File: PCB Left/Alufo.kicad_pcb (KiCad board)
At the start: 2 copper layers, 282.6 x 90.9 mm, 91 parts, among them J1 USB_C_Receptacle_USB2.0_16P_2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, J3 USB_C_Receptacle_USB2.0_16P_2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, K11 PG1350, K12 PG1350, K13 PG1350, K14 PG1350, K15 PG1350, K16 PG1350, K21 PG1350, K22 PG1350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

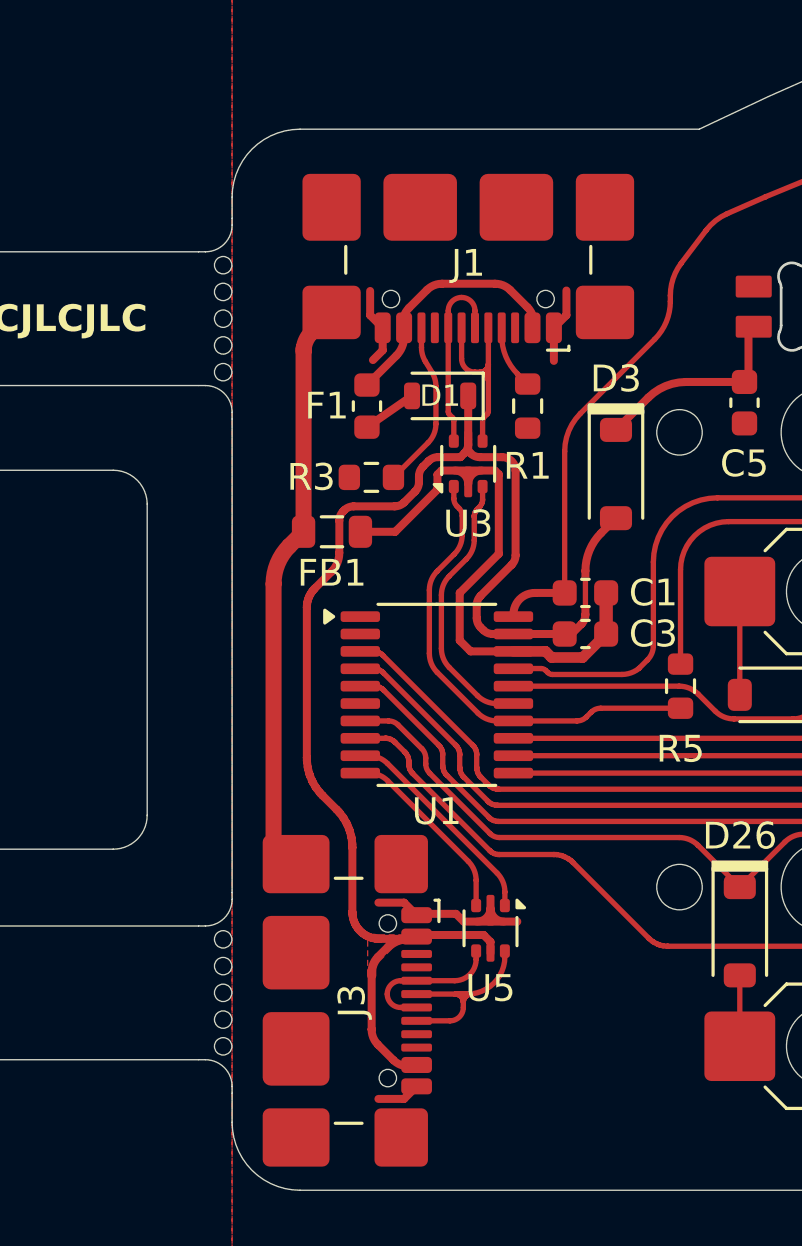
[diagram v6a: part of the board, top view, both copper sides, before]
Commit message: Update extra USB port solder pad
The pad should now not overlap with parts of the port casing that have no metal.
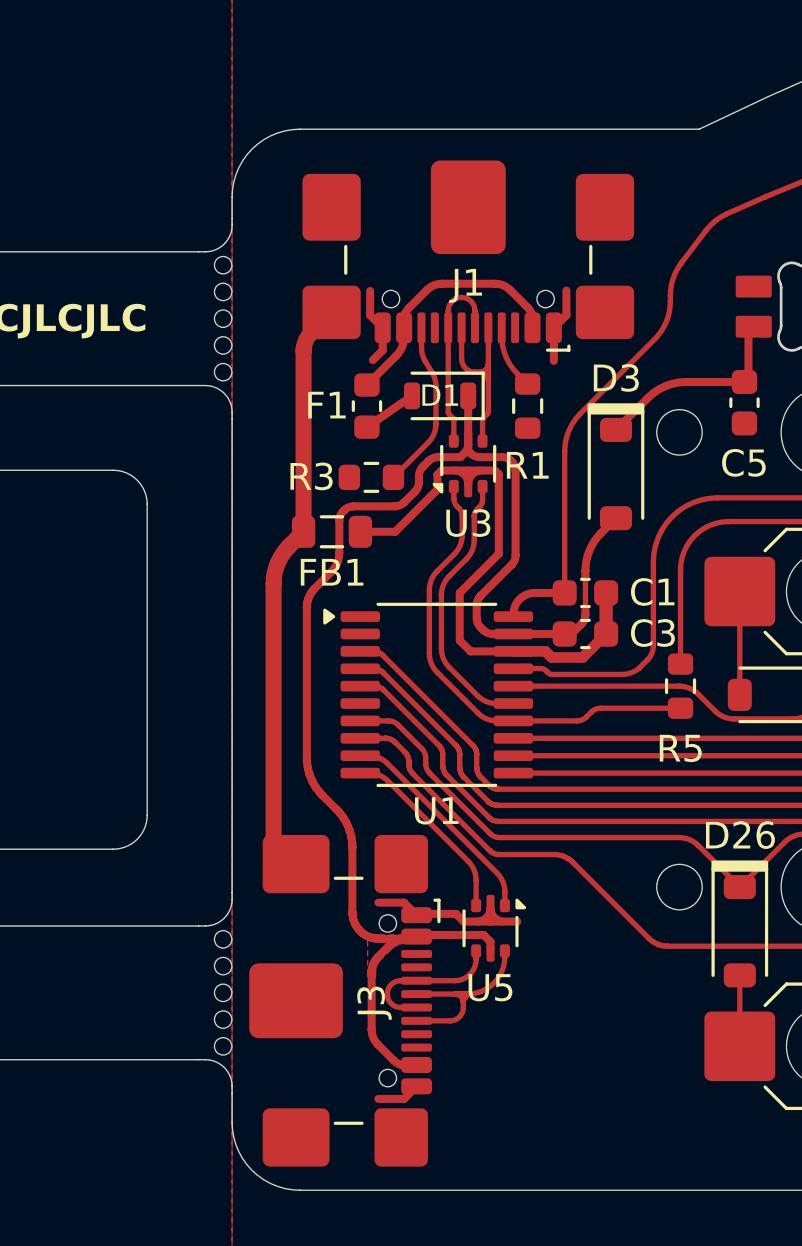
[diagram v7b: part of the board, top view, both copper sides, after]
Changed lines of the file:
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@@
 		(tags "USB 2.0 C Type-C Receptacle SMD 16P 16C USB4110-GF-A")
 		(property "Reference" "J1"
-			(at 0 -1.27 0)
+			(at 0 -2.015 0)
 			(unlocked yes)
 			(layer "F.SilkS")
@@
 			)
 		)
-		(property "Datasheet" "https://www.usb.org/sites/default/files/documents/usb_type-c.zip"
+		(property "Datasheet" ""
 			(at 0 0 180)
 			(unlocked yes)
@@
 			)
 		)
-		(property "Description" "USB 2.0-only 16P Type-C Receptacle connector"
+		(property "Description" ""
 			(at 0 0 180)
 			(unlocked yes)
@@
 			)
 		)
-		(property "LCSC" "C2681552"
-			(at 0 0 180)
-			(unlocked yes)
-			(layer "F.Fab")
-			(hide yes)
-			(effects
-				(font
-					(size 1 1)
-					(thickness 0.15)
-				)
-			)
-		)
 		(property ki_fp_filters "USB*C*Receptacle*")
 		(sheetname "/")
@@
 		)
 		(pad "" smd roundrect
-			(at -1.798333 0.825 180)
-			(size 2.75 2.5)
-			(layers "F.Cu" "F.Mask" "F.Paste")
-			(roundrect_rratio 0.125)
-			(thermal_bridge_angle 45)
-		)
-		(pad "" smd roundrect
-			(at 1.798333 0.825 180)
-			(size 2.75 2.5)
+			(at 0 0.825 180)
+			(size 2.8 3.5)
 			(layers "F.Cu" "F.Mask" "F.Paste")
 			(roundrect_rratio 0.125)
@@
 		(tags "USB 2.0 C Type-C Receptacle SMD 16P 16C USB4110-GF-A")
 		(property "Reference" "J3"
-			(at 0 -1.27 90)
+			(at 0 -2.015 90)
 			(unlocked yes)
 			(layer "F.SilkS")
@@
 			)
 		)
-		(property "Datasheet" "https://www.usb.org/sites/default/files/documents/usb_type-c.zip"
+		(property "Datasheet" ""
 			(at 0 0 270)
 			(unlocked yes)
@@
 			)
 		)
-		(property "Description" "USB 2.0-only 16P Type-C Receptacle connector"
+		(property "Description" ""
 			(at 0 0 270)
 			(unlocked yes)
@@
 			)
 		)
-		(property "LCSC" "C2681552"
-			(at 0 0 270)
-			(unlocked yes)
-			(layer "F.Fab")
-			(hide yes)
-			(effects
-				(font
-					(size 1 1)
-					(thickness 0.15)
-				)
-			)
-		)
 		(property ki_fp_filters "USB*C*Receptacle*")
 		(sheetname "/")
@@
 		)
 		(pad "" smd roundrect
-			(at -1.798333 0.825 270)
-			(size 2.75 2.5)
-			(layers "F.Cu" "F.Mask" "F.Paste")
-			(roundrect_rratio 0.125)
-			(thermal_bridge_angle 45)
-		)
-		(pad "" smd roundrect
-			(at 1.798333 0.825 270)
-			(size 2.75 2.5)
+			(at 0 0.825 270)
+			(size 2.8 3.5)
 			(layers "F.Cu" "F.Mask" "F.Paste")
 			(roundrect_rratio 0.125)

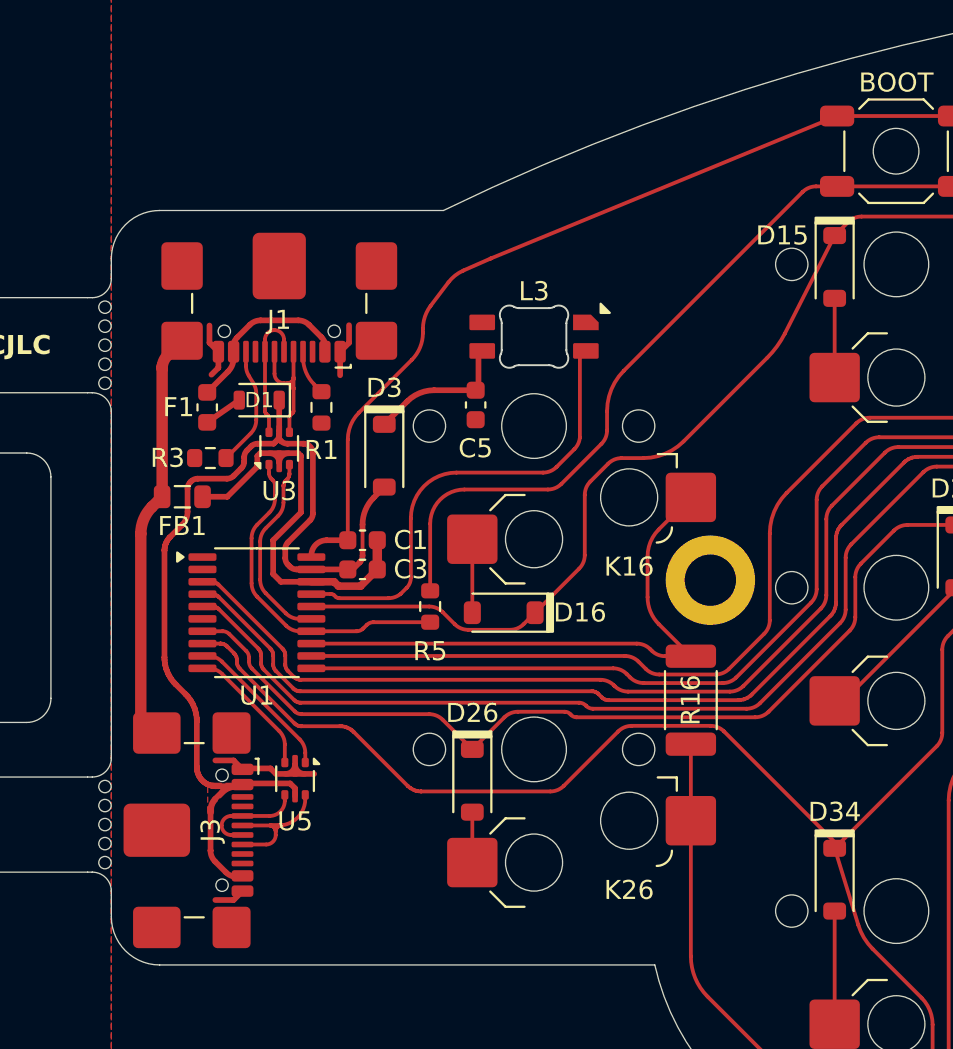
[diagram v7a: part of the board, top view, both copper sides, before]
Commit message: Add shield connectors
The USB ports will now be connected to the aluminium PCB core. This is done using a 0.6mm diameter wire. One end of the wire will be soldered to a pad on the PCB and the other will pass through a hole to friction fit against the aluminium core.

Also, R9, the 0Ω resistor on the lefthand VCC line has returned to allow a more direct ground route between the USB port and the MCU. However it is now a smaller 0805 size resistor.
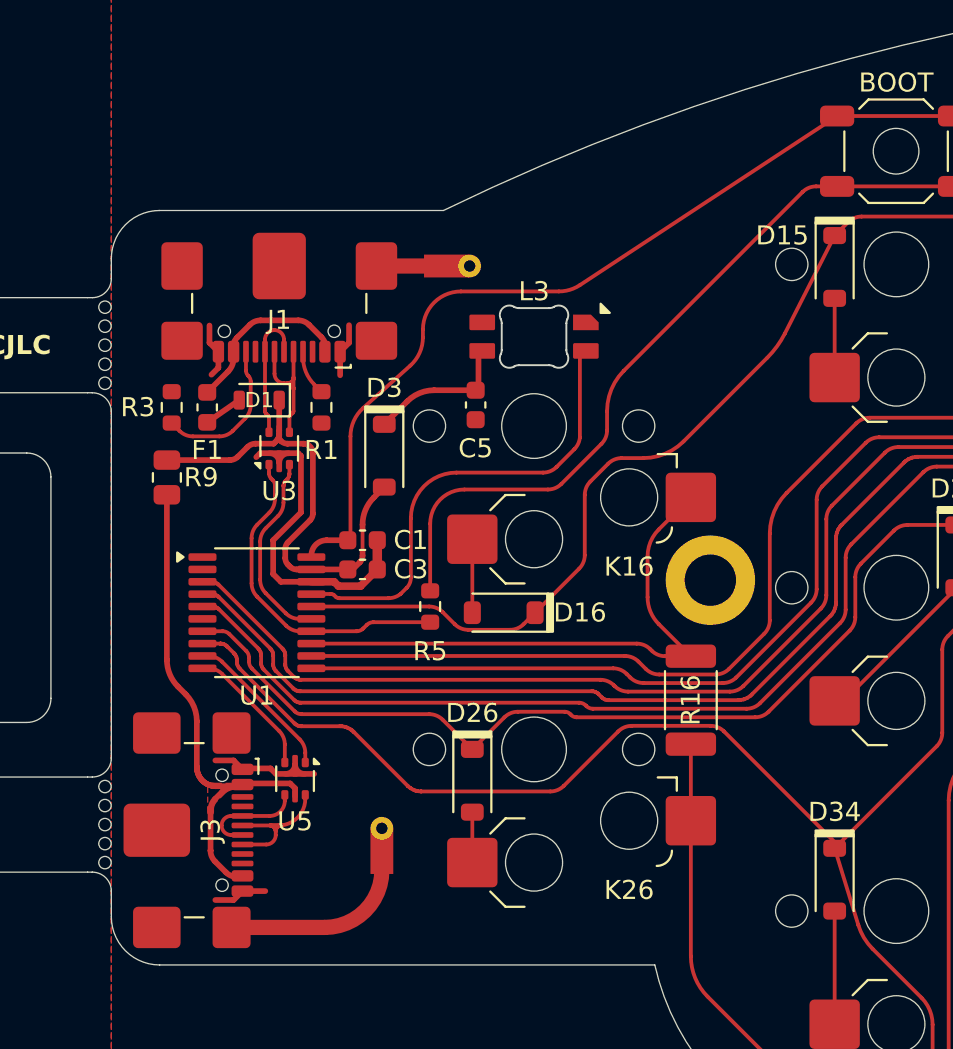
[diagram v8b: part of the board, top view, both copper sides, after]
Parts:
- removed FB1: FerriteBead, Inductor_SMD:L_0805_2012Metric
- added J5: Shield_Connection, Project_Library:Shield_Connector, F.Cu at (186.2, 44.0)
- added J7: Shield_Connection, Project_Library:Shield_Connector, F.Cu at (182.5, 74.5)
- added R9: 0R, Resistor_SMD:R_0805_2012Metric, F.Cu at (171.2, 55.1)
- moved R3 3.35 mm to (171.4, 51.4), turned to 90 degrees
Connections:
- J1 pad S1: SHIELD -> unconnected-(J1-SHIELD-PadS1)
- J1 pad S3: unconnected-(J1-SHIELD-PadS3) -> Net-(J5-Pin_1)
- J3 pad A4: VCC -> VCC'
- J3 pad A9: VCC -> VCC'
- J3 pad B4: VCC -> VCC'
- J3 pad B9: VCC -> VCC'
- J3 pad S1: unconnected-(J3-SHIELD-PadS1) -> Net-(J7-Pin_1)
- J3 pad S3: SHIELD -> unconnected-(J3-SHIELD-PadS3)
- U5 pad 5: VCC -> VCC'
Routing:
- net VCC: track 52.2 -> 25.3 mm
- net VCC': track 0.00 -> 26.3 mm
- net SHIELD: track 21.9 -> 0.00 mm
- net Net-(J7-Pin_1): track 0.00 -> 9.90 mm
- net Net-(J5-Pin_1): track 0.00 -> 3.70 mm
- net GND: track 29.5 -> 26.7 mm
- net Net-(J1-CC2): track 6.32 -> 8.09 mm
- added copper zone on F.Cu, net VCC'
- removed copper zone on F.Cu, net VCC
